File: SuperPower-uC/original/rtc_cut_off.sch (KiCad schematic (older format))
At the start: 10 parts, among them J601 Conn_01x02_Male, U601 RV-3028-C7

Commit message: Fix ERC and annotated the missing symbols (no fresh annotation)
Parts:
- gave numbers to parts that had none: 2
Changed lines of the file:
@@
 	6500 2500 6900 2500
 $Comp
-L Device:Q_NMOS_DGS Q?
+L Device:Q_NMOS_DGS Q7
 U 1 1 5FCB2D78
 P 6800 3350
-F 0 "Q?" H 7004 3396 50  0000 L CNN
+F 0 "Q7" H 7004 3396 50  0000 L CNN
 F 1 "Q_NMOS_DGS" H 7004 3305 50  0000 L CNN
 F 2 "" H 7000 3450 50  0001 C CNN
@@
 $EndComp
 $Comp
-L power:GND #PWR?
+L power:GND #PWR0114
 U 1 1 5FCB73B1
 P 6900 3650
-F 0 "#PWR?" H 6900 3400 50  0001 C CNN
+F 0 "#PWR0114" H 6900 3400 50  0001 C CNN
 F 1 "GND" H 6905 3477 50  0000 C CNN
 F 2 "" H 6900 3650 50  0001 C CNN
@@
 	6900 3050 7200 3050
 $Comp
-L Device:R R?
+L Device:R R15
 U 1 1 5FCCE813
 P 6900 2800
-F 0 "R?" H 6850 2750 50  0000 R CNN
+F 0 "R15" H 6850 2750 50  0000 R CNN
 F 1 "100k" H 6850 2850 50  0000 R CNN
 F 2 "Resistors_SMD:R_0603" V 6830 2800 50  0001 C CNN

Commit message: Signal N-MOSFET update
Update signal N-MOSFET symbols by 2N7002A (x3)
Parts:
- removed Q7: Q_NMOS_DGS, symbol Device:Q_NMOS_DGS
- added Q7: 2N7002A, Package_TO_SOT_SMD:SOT-23, symbol 2n7002a:2N7002A
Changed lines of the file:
@@
 $Descr A4 11693 8268
 encoding utf-8
-Sheet 6 7
+Sheet 5 7
 Title "SuperPower-uC"
 Date "2020-09-20"
@@
 	6500 2500 6900 2500
 $Comp
-L Device:Q_NMOS_DGS Q7
-U 1 1 5FCB2D78
-P 6800 3350
-F 0 "Q7" H 7004 3396 50  0000 L CNN
-F 1 "Q_NMOS_DGS" H 7004 3305 50  0000 L CNN
-F 2 "" H 7000 3450 50  0001 C CNN
-F 3 "~" H 6800 3350 50  0001 C CNN
-	1    6800 3350
-	1    0    0    -1
-$EndComp
-$Comp
 L power:GND #PWR0114
 U 1 1 5FCB73B1
@@
 Wire Wire Line
 	6900 2500 7800 2500
+$Comp
+L 2n7002a:2N7002A Q7
+U 1 1 5FCC1CED
+P 6800 3350
+F 0 "Q7" H 7005 3487 50  0000 L CNN
+F 1 "2N7002A" H 7005 3396 50  0000 L CNN
+F 2 "Package_TO_SOT_SMD:SOT-23" H 7000 3275 50  0001 L CNN
+F 3 "https://www.diodes.com/assets/Datasheets/ds31360.pdf" H 6800 3350 50  0001 C CNN
+F 4 "Diodes Incorporated" H 6800 3350 50  0001 C CNN "Mfr_name"
+F 5 "2N7002A-7" H 6800 3350 50  0001 C CNN "Mfr_no"
+F 6 "SOT23-3" H 7005 3305 50  0000 L CNN "Package"
+F 7 "60V" H 6800 3350 50  0001 C CNN "VDSS"
+F 8 "6Ω" H 7005 3214 50  0000 L CNN "RDSon"
+F 9 "220mA" H 6800 3350 50  0001 C CNN "IDmax"
+F 10 "1.2-2.0V" H 6800 3350 50  0001 C CNN "VGSth"
+F 11 "20V" H 6800 3350 50  0001 C CNN "VGSS"
+F 12 "https://octopart.com/2n7002a-7-diodes+inc.-12411377?r=sp" H 6800 3350 50  0001 C CNN "Octopart_link"
+F 13 "https://fr.farnell.com/diodes-inc/2n7002a-7/mosfet-canal-n-60v-0-18a-sot-23/dp/3127180?st=2n7002a-7" H 6800 3350 50  0001 C CNN "Farnell_link"
+F 14 "3127180" H 6800 3350 50  0001 C CNN "Farnell_ref"
+F 15 "2020-12-04" H 6800 3350 50  0001 C CNN "Farnell_check_date"
+F 16 "0,211 €" H 6800 3350 50  0001 C CNN "Farnell_price_qt=5"
+F 17 "0,209 €" H 6800 3350 50  0001 C CNN "Farnell_price_qt=25"
+F 18 "0,0964 €" H 6800 3350 50  0001 C CNN "Farnell_price_qt=100"
+F 19 "0,0904 €" H 6800 3350 50  0001 C CNN "Farnell_price_qt=250"
+F 20 "2,238" H 6800 3350 50  0001 C CNN "Farnell_stock"
+F 21 "https://lcsc.com/product-detail/MOSFET_Diodes-Incorporated-2N7002A-7_C139446.html" H 6800 3350 50  0001 C CNN "LCSC_link"
+F 22 "C139446" H 6800 3350 50  0001 C CNN "LCSC_ref"
+F 23 "2020-12-04" H 6800 3350 50  0001 C CNN "LCSC_check_date"
+F 24 "$0.0247" H 6800 3350 50  0001 C CNN "LCSC_price_qt=20"
+F 25 "$0.0184" H 6800 3350 50  0001 C CNN "LCSC_price_qt=200"
+F 26 "$0.0173" H 6800 3350 50  0001 C CNN "LCSC_price_qt=600"
+F 27 "$0.0161" H 6800 3350 50  0001 C CNN "LCSC_price_qt=2000"
+F 28 "20,880" H 6800 3350 50  0001 C CNN "LCSC_stock"
+F 29 "https://eu.mouser.com/ProductDetail/Diodes-Incorporated/2N7002A-7?qs=%2Fha2pyFaduiVkHzHToHS9vYfqHI9tbd78Fpui8SRcmA=" H 6800 3350 50  0001 C CNN "Mouser_link"
+F 30 "621-2N7002A-7" H 6800 3350 50  0001 C CNN "Mouser_ref"
+F 31 "$0.293" H 6800 3350 50  0001 C CNN "Mouser_price_qt=1"
+F 32 "$0.201" H 6800 3350 50  0001 C CNN "Mouser_price_qt=10"
+F 33 "$0.096" H 6800 3350 50  0001 C CNN "Mouser_price_qt=100"
+F 34 "$0.082" H 6800 3350 50  0001 C CNN "Mouser_price_qt=500"
+F 35 "2020-12-04" H 6800 3350 50  0001 C CNN "Mouser_check_date"
+F 36 "21,482" H 6800 3350 50  0001 C CNN "Mouser_stock"
+F 37 "https://fr.rs-online.com/web/p/transistors-mosfet/8228647/" H 6800 3350 50  0001 C CNN "RS_link"
+F 38 "822-8647" H 6800 3350 50  0001 C CNN "RS_ref"
+F 39 "2020-12-04" H 6800 3350 50  0001 C CNN "RS_check_date"
+F 40 "0,079 €" H 6800 3350 50  0001 C CNN "RS_price_qt=150"
+F 41 "1800" H 6800 3350 50  0001 C CNN "RS_stock"
+F 42 "TO_CHECK" H 6800 3350 50  0001 C CNN "Status"
+F 43 "1.00" H 6800 3350 50  0001 C CNN "Release_version"
+F 44 "2020-12-03" H 6800 3350 50  0001 C CNN "Release_date"
+F 45 "ManWithNoName" H 6800 3350 50  0001 C CNN "Designer"
+	1    6800 3350
+	1    0    0    -1
+$EndComp
 $EndSCHEMATC

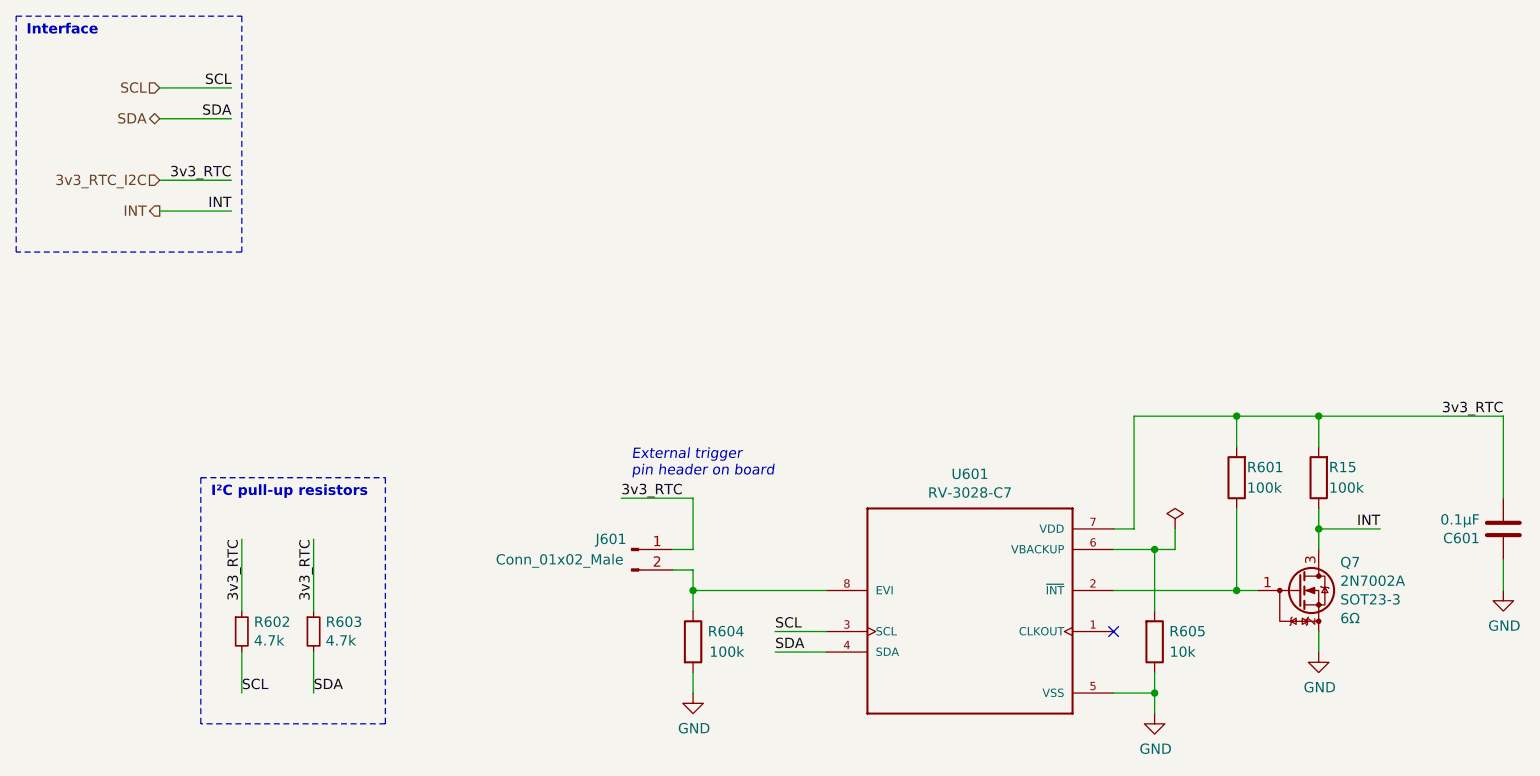
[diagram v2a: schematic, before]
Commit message: Add tactile-button to rtc sheet (DNP)
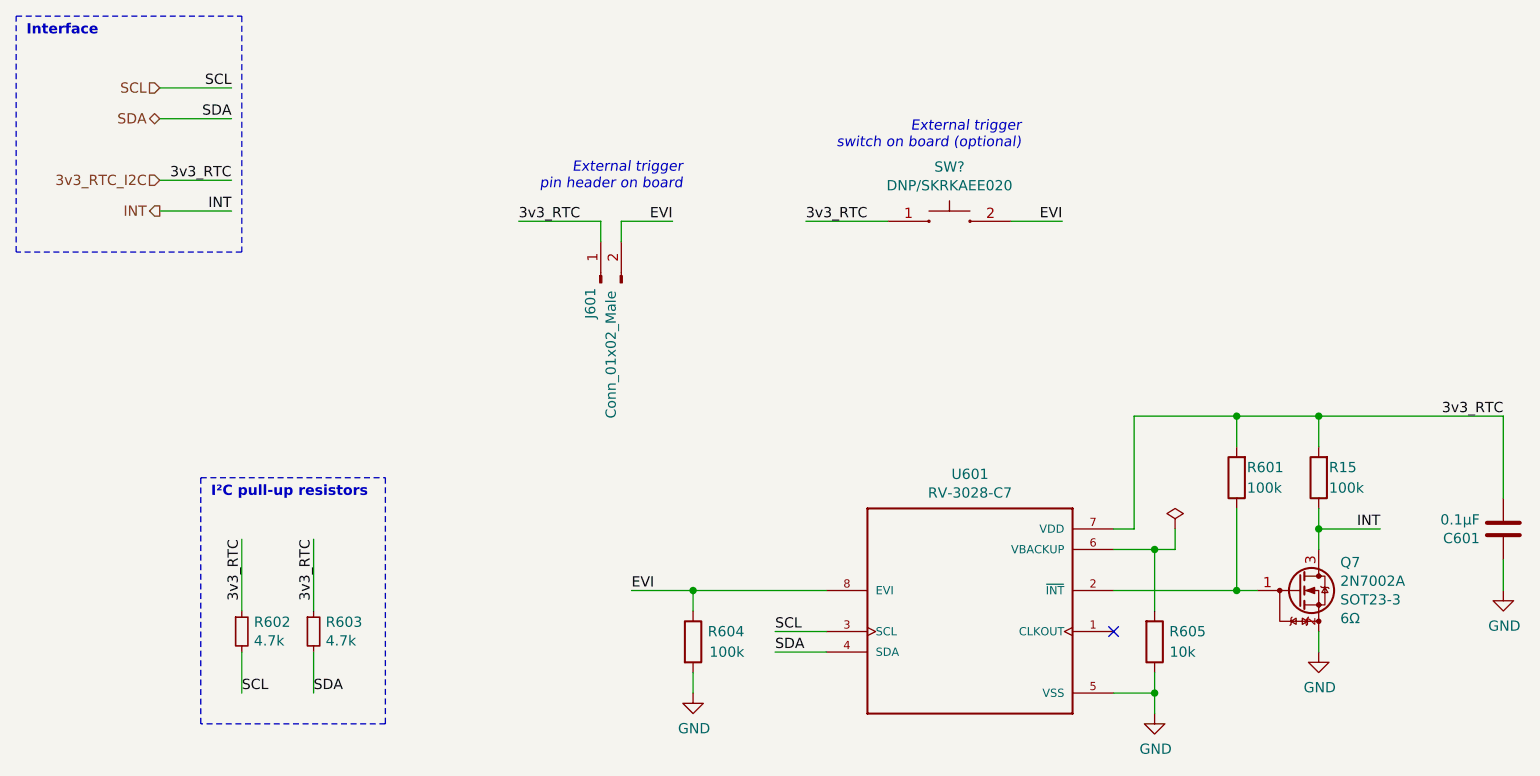
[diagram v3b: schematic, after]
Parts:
- added SW?: DNP/SKRKAEE020, symbol SKRKAEE020:SKRKAEE020
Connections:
- net 3v3_RTC_I2C: now also SW?.1
- net EVI: now reaches J601.2 (Pin_2), R604.1, U601.8 (EVI)
- net EVI: now also SW?.2
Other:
- note added: "External trigger\nswitch on board (optional)"
- moved on the sheet: J601
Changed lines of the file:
@@
 	5900 3850 6100 3850
 Wire Wire Line
-	3750 3250 3850 3250
-Wire Wire Line
-	3750 3150 3850 3150
+	3500 1650 3500 1550
+Wire Wire Line
+	3400 1650 3400 1550
 Wire Wire Line
 	3850 3750 3850 3850
@@
 L Connector:Conn_01x02_Male J601
 U 1 1 5F78D93A
-P 3550 3150
-F 0 "J601" H 3450 3200 50  0000 C CNN
-F 1 "Conn_01x02_Male" H 3200 3100 50  0000 C CNN
-F 2 "" H 3550 3150 50  0001 C CNN
-F 3 "~" H 3550 3150 50  0001 C CNN
-	1    3550 3150
-	1    0    0    -1
+P 3400 1850
+F 0 "J601" H 3300 1900 50  0000 C CNN
+F 1 "Conn_01x02_Male" H 3050 1800 50  0000 C CNN
+F 2 "" H 3400 1850 50  0001 C CNN
+F 3 "~" H 3400 1850 50  0001 C CNN
+	1    3400 1850
+	0    -1   -1   0
 $EndComp
 $Comp
@@
 	1    0    0    -1
 $EndComp
-Wire Wire Line
-	3850 3250 3850 3350
 Wire Wire Line
 	4500 3350 3850 3350
@@
 Text Label 7800 2500 2    50   ~ 0
 3v3_RTC
-Wire Wire Line
-	3850 2900 3850 3150
-Text Label 3500 2900 0    50   ~ 0
-3v3_RTC
-Text Notes 3550 2800 0    50   Italic 0
+Text Label 3000 1550 0    50   ~ 0
+3v3_RTC
+Text Notes 3800 1400 2    50   Italic 0
 External trigger\npin header on board
 Text Label 2000 3100 3    50   ~ 0
@@
 Wire Notes Line
 	550  1700 550  550
-Wire Wire Line
-	3500 2900 3850 2900
 Wire Wire Line
 	6500 2500 6900 2500
@@
 	1    0    0    -1
 $EndComp
+$Comp
+L SKRKAEE020:SKRKAEE020 SW?
+U 1 1 5FCD718C
+P 5100 1550
+F 0 "SW?" H 5100 1815 50  0000 C CNN
+F 1 "DNP/SKRKAEE020" H 5100 1724 50  0000 C CNN
+F 2 "" H 5100 1550 50  0001 C CNN
+F 3 "" H 5100 1550 50  0001 C CNN
+	1    5100 1550
+	1    0    0    -1
+$EndComp
+Text Label 3550 3350 0    50   ~ 0
+EVI
+Wire Wire Line
+	3550 3350 3850 3350
+Text Label 3750 1550 2    50   ~ 0
+EVI
+Wire Wire Line
+	3500 1550 3750 1550
+Text Label 5650 1550 2    50   ~ 0
+EVI
+Text Label 4400 1550 0    50   ~ 0
+3v3_RTC
+Wire Wire Line
+	4400 1550 4800 1550
+Wire Wire Line
+	5400 1550 5650 1550
+Wire Wire Line
+	3000 1550 3400 1550
+Text Notes 5450 1200 2    50   Italic 0
+External trigger\nswitch on board (optional)
 $EndSCHEMATC

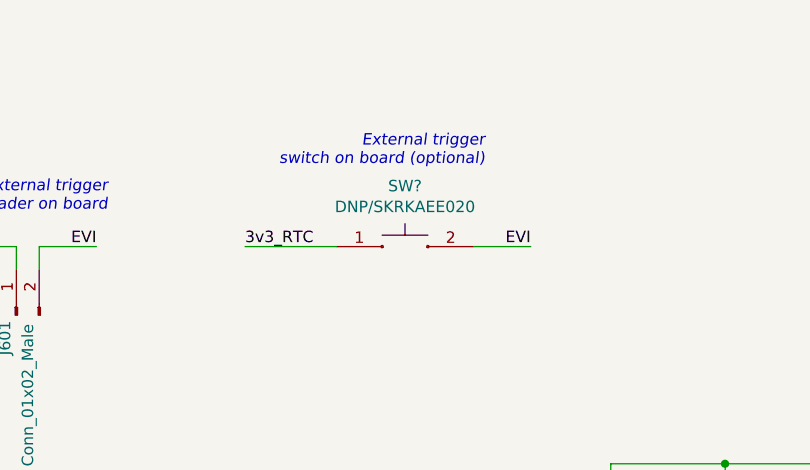
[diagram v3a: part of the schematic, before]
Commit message: Exchanged the USB-C symbol and footprint with connector usb4110
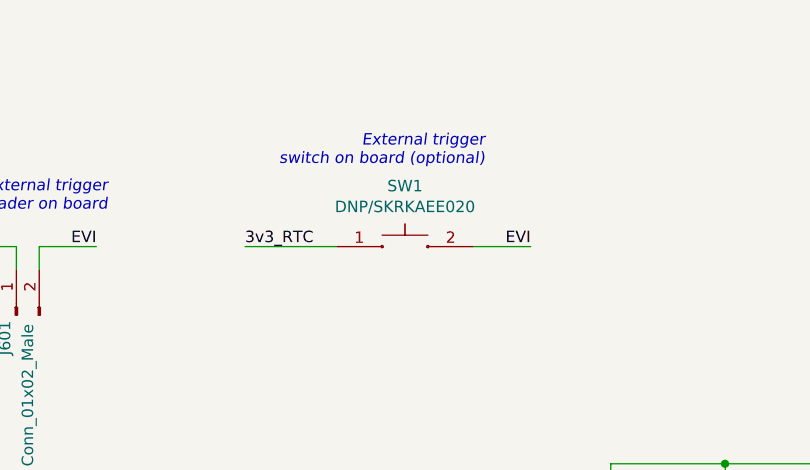
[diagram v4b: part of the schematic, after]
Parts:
- gave numbers to parts that had none: 1
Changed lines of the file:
@@
 $EndComp
 $Comp
-L SKRKAEE020:SKRKAEE020 SW?
+L SKRKAEE020:SKRKAEE020 SW1
 U 1 1 5FCD718C
 P 5100 1550
-F 0 "SW?" H 5100 1815 50  0000 C CNN
+F 0 "SW1" H 5100 1815 50  0000 C CNN
 F 1 "DNP/SKRKAEE020" H 5100 1724 50  0000 C CNN
 F 2 "" H 5100 1550 50  0001 C CNN

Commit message: Assigned footprint to resistors 0603 and connectors
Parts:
- J601: footprint (none) -> Connector_PinSocket_2.54mm:PinSocket_1x02_P2.54mm_Vertical
- SW1: footprint (none) -> SKRKAEE020:SKRKAEE020
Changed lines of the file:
@@
 F 0 "J601" H 3300 1900 50  0000 C CNN
 F 1 "Conn_01x02_Male" H 3050 1800 50  0000 C CNN
-F 2 "" H 3400 1850 50  0001 C CNN
+F 2 "Connector_PinSocket_2.54mm:PinSocket_1x02_P2.54mm_Vertical" H 3400 1850 50  0001 C CNN
 F 3 "~" H 3400 1850 50  0001 C CNN
 	1    3400 1850
@@
 F 0 "SW1" H 5100 1815 50  0000 C CNN
 F 1 "DNP/SKRKAEE020" H 5100 1724 50  0000 C CNN
-F 2 "" H 5100 1550 50  0001 C CNN
+F 2 "SKRKAEE020:SKRKAEE020" H 5100 1550 50  0001 C CNN
 F 3 "" H 5100 1550 50  0001 C CNN
 	1    5100 1550

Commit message: Updated footprints and fixed issues
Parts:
- Q7: footprint Package_TO_SOT_SMD:SOT-23 -> TO_SOT_Packages_SMD:SOT-23
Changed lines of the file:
@@
 F 0 "Q7" H 7005 3487 50  0000 L CNN
 F 1 "2N7002A" H 7005 3396 50  0000 L CNN
-F 2 "Package_TO_SOT_SMD:SOT-23" H 7000 3275 50  0001 L CNN
+F 2 "TO_SOT_Packages_SMD:SOT-23" H 7000 3275 50  0001 L CNN
 F 3 "https://www.diodes.com/assets/Datasheets/ds31360.pdf" H 6800 3350 50  0001 C CNN
 F 4 "Diodes Incorporated" H 6800 3350 50  0001 C CNN "Mfr_name"

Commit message: reassigned most footprints
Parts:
- C601: footprint Capacitors_SMD:C_0603 -> Capacitor_SMD:C_0603_1608Metric
- Q7: footprint TO_SOT_Packages_SMD:SOT-23 -> Package_TO_SOT_SMD:SOT-23
- R15, R601, R602, R603, R604, R605: footprint Resistors_SMD:R_0603 -> Resistor_SMD:R_0603_1608Metric
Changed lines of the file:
@@
 F 0 "R605" H 6350 3550 50  0000 R CNN
 F 1 "10k" H 6300 3650 50  0000 R CNN
-F 2 "Resistors_SMD:R_0603" V 6030 3600 50  0001 C CNN
+F 2 "Resistor_SMD:R_0603_1608Metric" V 6030 3600 50  0001 C CNN
 F 3 "~" H 6100 3600 50  0001 C CNN
 	1    6100 3600
@@
 F 0 "R601" H 6450 2750 50  0000 R CNN
 F 1 "100k" H 6450 2850 50  0000 R CNN
-F 2 "Resistors_SMD:R_0603" V 6430 2800 50  0001 C CNN
+F 2 "Resistor_SMD:R_0603_1608Metric" V 6430 2800 50  0001 C CNN
 F 3 "~" H 6500 2800 50  0001 C CNN
 	1    6500 2800
@@
 F 0 "C601" H 7915 3096 50  0000 L CNN
 F 1 "0.1µF" H 7915 3005 50  0000 L CNN
-F 2 "Capacitors_SMD:C_0603" H 7838 2900 50  0001 C CNN
+F 2 "Capacitor_SMD:C_0603_1608Metric" H 7838 2900 50  0001 C CNN
 F 3 "~" H 7800 3050 50  0001 C CNN
 	1    7800 3050
@@
 F 0 "R604" H 4100 3650 50  0000 R CNN
 F 1 "100k" H 4100 3550 50  0000 R CNN
-F 2 "Resistors_SMD:R_0603" V 3780 3600 50  0001 C CNN
+F 2 "Resistor_SMD:R_0603_1608Metric" V 3780 3600 50  0001 C CNN
 F 3 "~" H 3850 3600 50  0001 C CNN
 	1    3850 3600
@@
 F 0 "R603" H 2059 3596 50  0000 L CNN
 F 1 "4.7k" H 2059 3505 50  0000 L CNN
-F 2 "Resistors_SMD:R_0603" H 2000 3550 50  0001 C CNN
+F 2 "Resistor_SMD:R_0603_1608Metric" H 2000 3550 50  0001 C CNN
 F 3 "~" H 2000 3550 50  0001 C CNN
 	1    2000 3550
@@
 F 0 "R602" H 1709 3596 50  0000 L CNN
 F 1 "4.7k" H 1709 3505 50  0000 L CNN
-F 2 "Resistors_SMD:R_0603" H 1650 3550 50  0001 C CNN
+F 2 "Resistor_SMD:R_0603_1608Metric" H 1650 3550 50  0001 C CNN
 F 3 "~" H 1650 3550 50  0001 C CNN
 	1    1650 3550
@@
 F 0 "R15" H 6850 2750 50  0000 R CNN
 F 1 "100k" H 6850 2850 50  0000 R CNN
-F 2 "Resistors_SMD:R_0603" V 6830 2800 50  0001 C CNN
+F 2 "Resistor_SMD:R_0603_1608Metric" V 6830 2800 50  0001 C CNN
 F 3 "~" H 6900 2800 50  0001 C CNN
 	1    6900 2800
@@
 F 0 "Q7" H 7005 3487 50  0000 L CNN
 F 1 "2N7002A" H 7005 3396 50  0000 L CNN
-F 2 "TO_SOT_Packages_SMD:SOT-23" H 7000 3275 50  0001 L CNN
+F 2 "Package_TO_SOT_SMD:SOT-23" H 7000 3275 50  0001 L CNN
 F 3 "https://www.diodes.com/assets/Datasheets/ds31360.pdf" H 6800 3350 50  0001 C CNN
 F 4 "Diodes Incorporated" H 6800 3350 50  0001 C CNN "Mfr_name"
